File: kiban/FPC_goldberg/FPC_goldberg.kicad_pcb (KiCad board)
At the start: 2 copper layers, 68.2 x 85.3 mm, 162 parts, among them J1 IN, J2 OUT

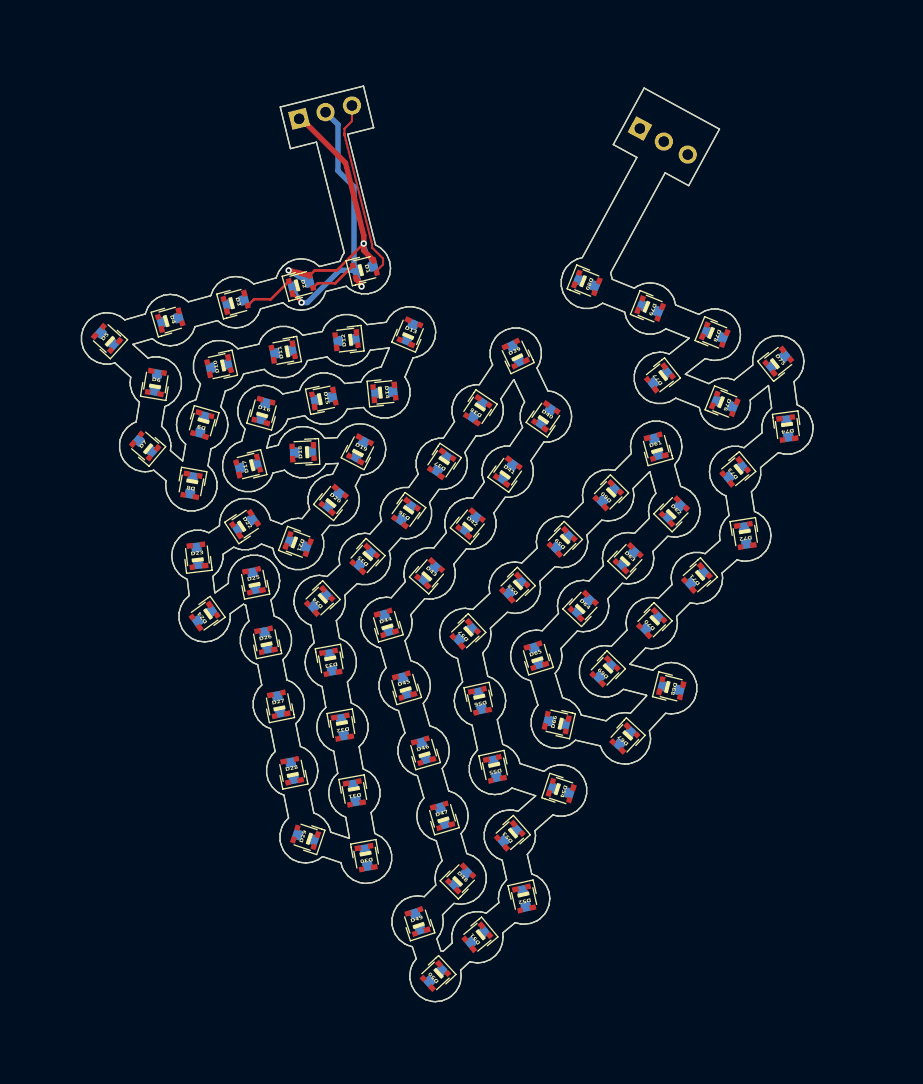
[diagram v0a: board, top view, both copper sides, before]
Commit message: fpc: island land radius 2.4→2.55mm; refresh c0 outline + board
ISLAND_R 2.55mm (diam 5.1mm) keeps a 0.18mm copper gap at the closest
non-adjacent island pair (centres 5.28mm) — within FPC min-spacing.
Regenerated fpc_outline_c0.json and redrew Edge.Cuts + F.SilkS on the
FPC_goldberg board (LED/cap positions unchanged).

Co-Authored-By: Claude Opus 4.8 (1M context) <noreply@anthropic.com>
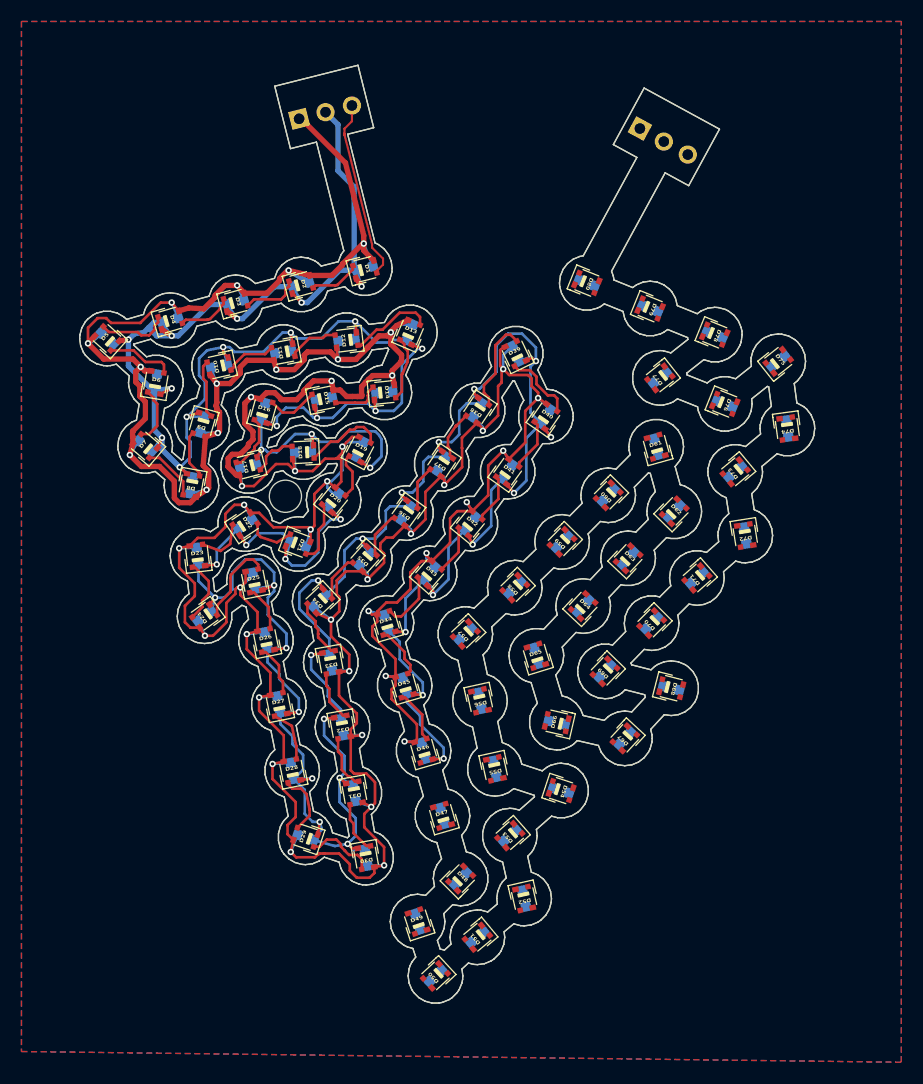
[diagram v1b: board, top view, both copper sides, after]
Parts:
- turned C10 to 12.435 degrees
- turned C11 to 10.627 degrees
- turned C13 to -113.042 degrees
- turned C14 to -174.2 degrees
- turned C15 to -168.258 degrees
- turned C16 to -105.523 degrees
- turned C17 to 14.133 degrees
- turned C19 to -117.551 degrees
- turned C20 to -128.894 degrees
- turned C21 to 159.421 degrees
- turned C22 to -146.42 degrees
- turned C23 to -83.223 degrees
- turned C24 to 35.634 degrees
- turned C25 to -78.653 degrees
- turned C26 to -78.637 degrees
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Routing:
- net +5V: track 28.5 -> 456.1 mm, vias 2 -> 46
- net GND: track 27.7 -> 429.6 mm, vias 2 -> 46
- net Net-(D38-DOUT): track 0.00 -> 8.86 mm
- net OUT3: track 0.00 -> 8.02 mm
- net Net-(D12-DOUT): track 0.00 -> 7.97 mm
- net Net-(D18-DOUT): track 0.00 -> 7.57 mm
- net Net-(D39-DOUT): track 0.00 -> 6.84 mm
- net Net-(D4-DOUT): track 0.00 -> 6.66 mm
- net Net-(D29-DOUT): track 0.00 -> 6.61 mm
- net Net-(D5-DOUT): track 0.00 -> 6.29 mm
- net Net-(D23-DOUT): track 0.00 -> 6.10 mm
- net Net-(D13-DOUT): track 0.00 -> 6.08 mm
- net Net-(D28-DOUT): track 0.00 -> 5.88 mm
- net Net-(D20-DOUT): track 0.00 -> 5.85 mm
- net Net-(D43-DOUT): track 0.00 -> 5.69 mm
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- added copper zone on F.Cu, net +5V
- added copper zone on B.Cu, net GND
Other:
- board size 68.2 x 85.3 mm -> 68.5 x 87.4 mm
